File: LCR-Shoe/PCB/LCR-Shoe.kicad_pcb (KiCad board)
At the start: 2 copper layers, 65 x 65 mm, 26 parts, among them J1 USB_B, J2 USB_C_Receptacle, J3 USB_B_Mini, J4 USB_B_Micro, J5 Conn_01x01_Female, J6 Conn_01x01_Male, Q1 IRLML6402PbF, U1 LM2731YMF, U2 LTC4412xS6

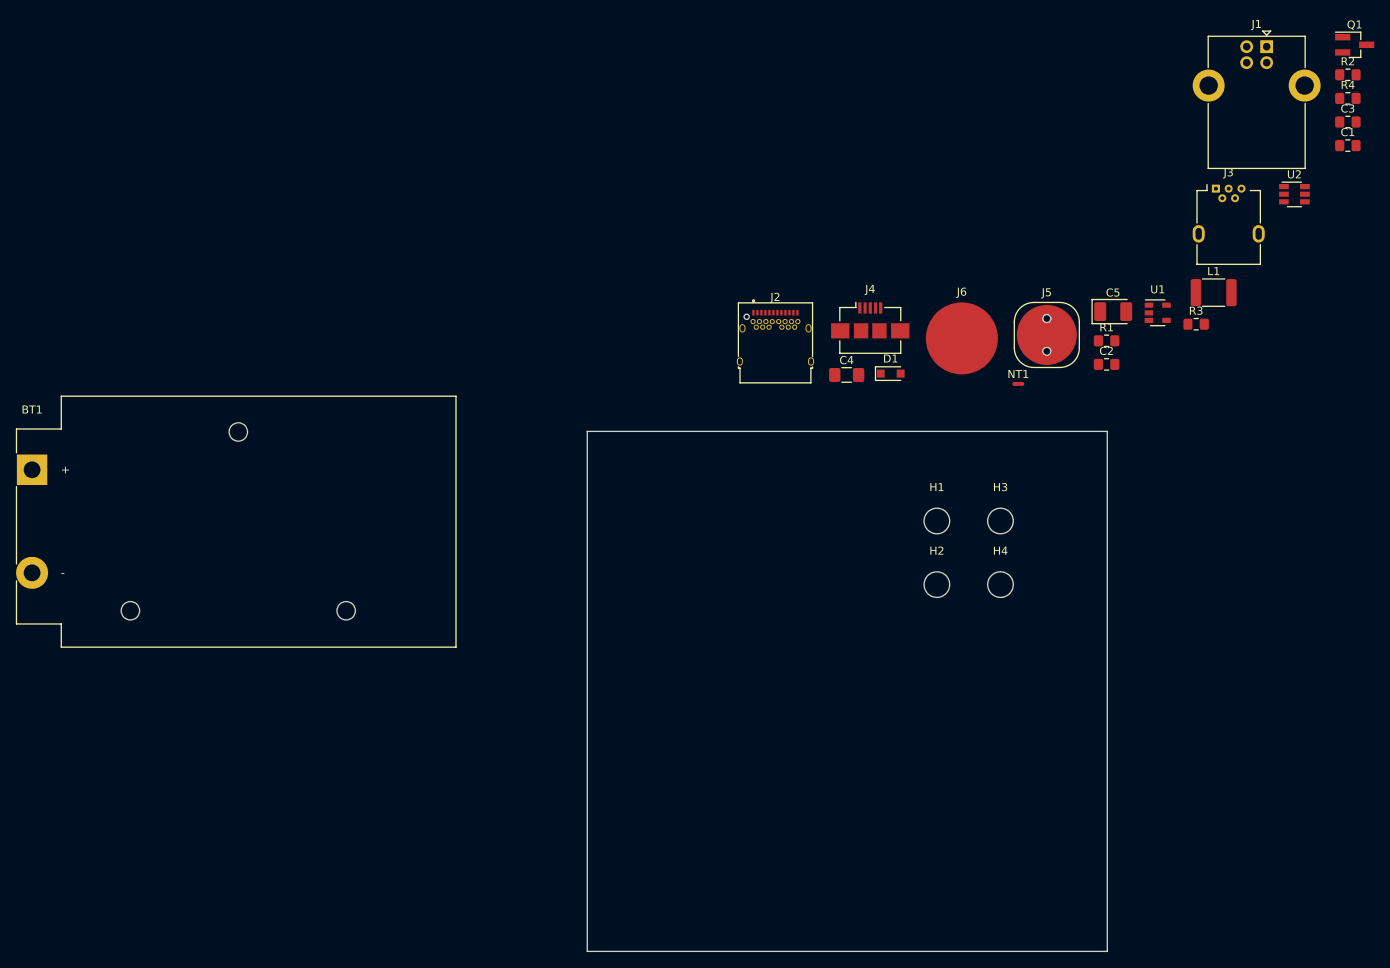
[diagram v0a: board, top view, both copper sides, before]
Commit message: All components laid out
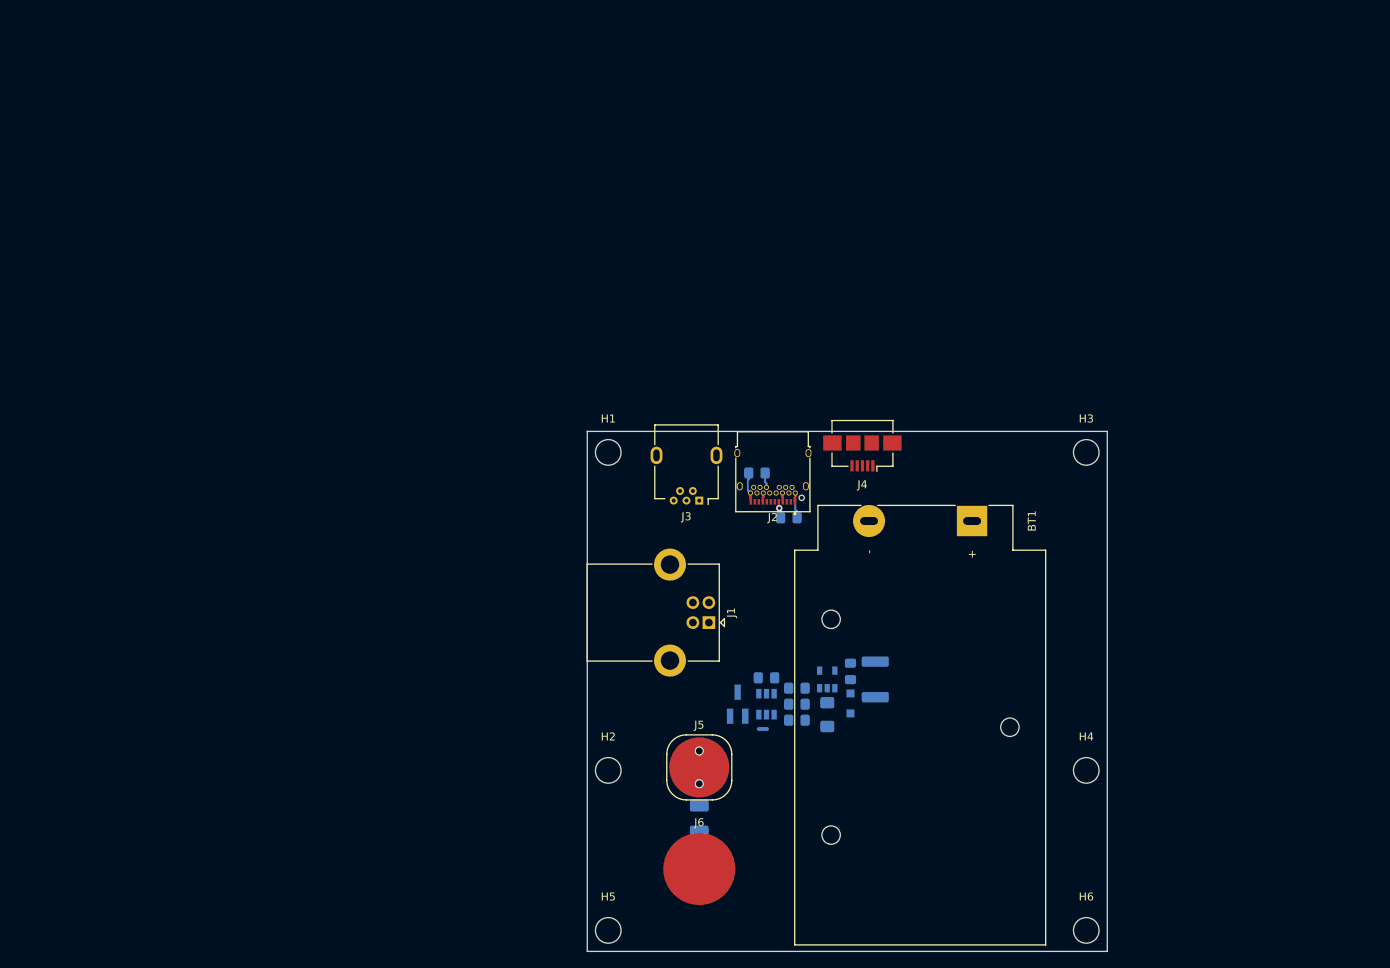
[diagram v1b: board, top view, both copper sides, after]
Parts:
- added H5: MountingHole, MountingHole:MountingHole_3.2mm_M3, F.Cu at (102.6, 162.4)
- added H6: MountingHole, MountingHole:MountingHole_3.2mm_M3, F.Cu at (162.4, 162.4)
- C1, C2, C3, C4, C5, D1, L1, NT1, Q1, R1, R2, R3, R4, U1, U2: moved to B.Cu
- moved BT1 117.7 mm to (148.1, 111.2), turned to 270 degrees
- moved Q1 112.9 mm to (118.8, 134.1), turned to 90 degrees
- moved R4 103.9 mm to (126.2, 136.1), turned to 180 degrees
- moved C3 100.5 mm to (122.4, 130.8)
- moved J1 100.2 mm to (115.2, 123.9), turned to 270 degrees
- moved U2 91.8 mm to (122.4, 134.1), turned to 270 degrees
- moved C1 90.5 mm to (132.9, 130.0), turned to 270 degrees
- moved R2 89.2 mm to (125.2, 110.8)
- moved C5 81.8 mm to (114.0, 148.4), turned to 270 degrees
- moved J3 75.4 mm to (114.0, 108.7), turned to 180 degrees
- moved J6 74.0 mm to (114.0, 154.7)
- moved J5 69.3 mm to (114.0, 142.0)
- moved R3 67.5 mm to (126.2, 132.1), turned to 180 degrees
- moved L1 64.2 mm to (136.0, 131.0), turned to 270 degrees
- moved U1 61.7 mm to (130.0, 131.0), turned to 90 degrees
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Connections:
- net Net-(J2-PadA5) renamed /USB_C-CC1
- net Net-(J2-PadB5) renamed /USB_C-CC2
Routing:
- net GND: track 0.00 -> 8.27 mm
- net +5V: track 0.00 -> 2.26 mm
- net /USB_C-CC1: track 0.00 -> 2.08 mm, vias 0 -> 1
- net /USB_C-CC2: track 0.00 -> 1.87 mm

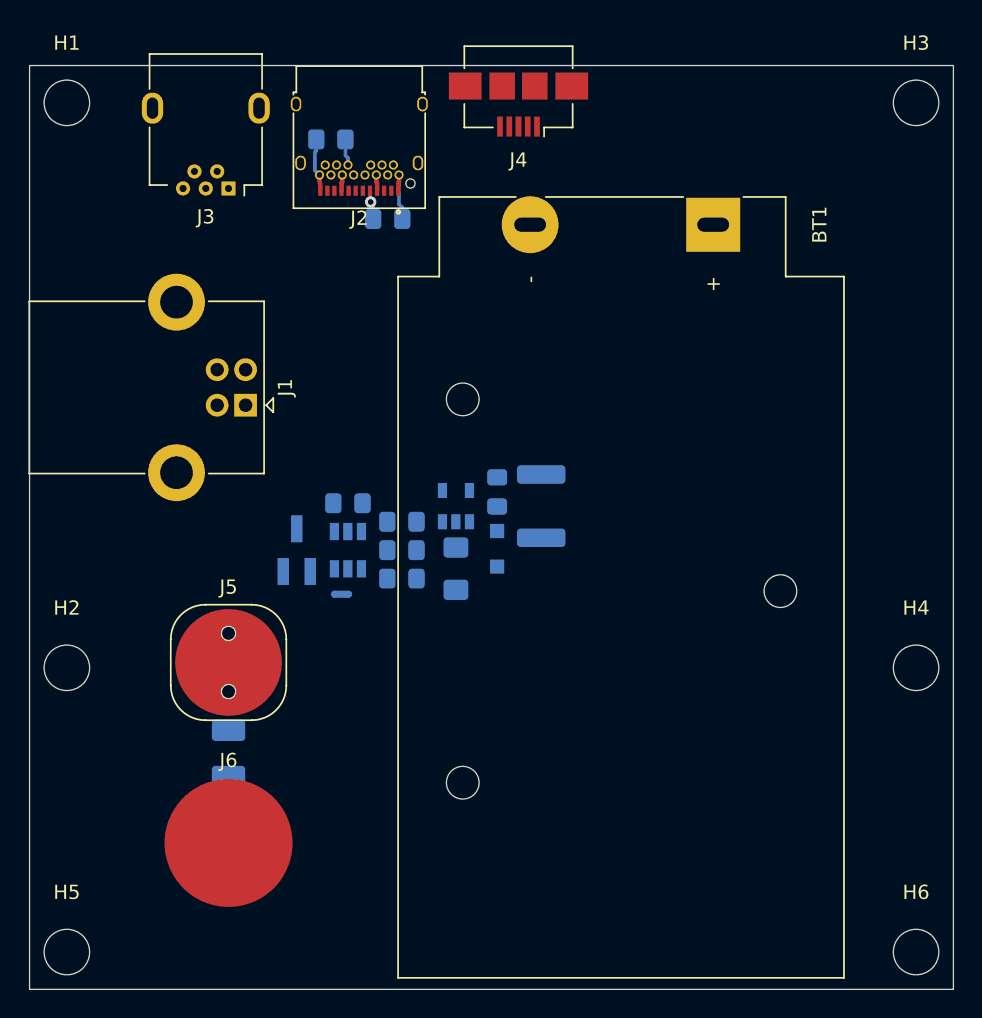
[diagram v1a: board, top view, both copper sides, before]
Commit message: Routing and positioning of the silk screen elements is finished
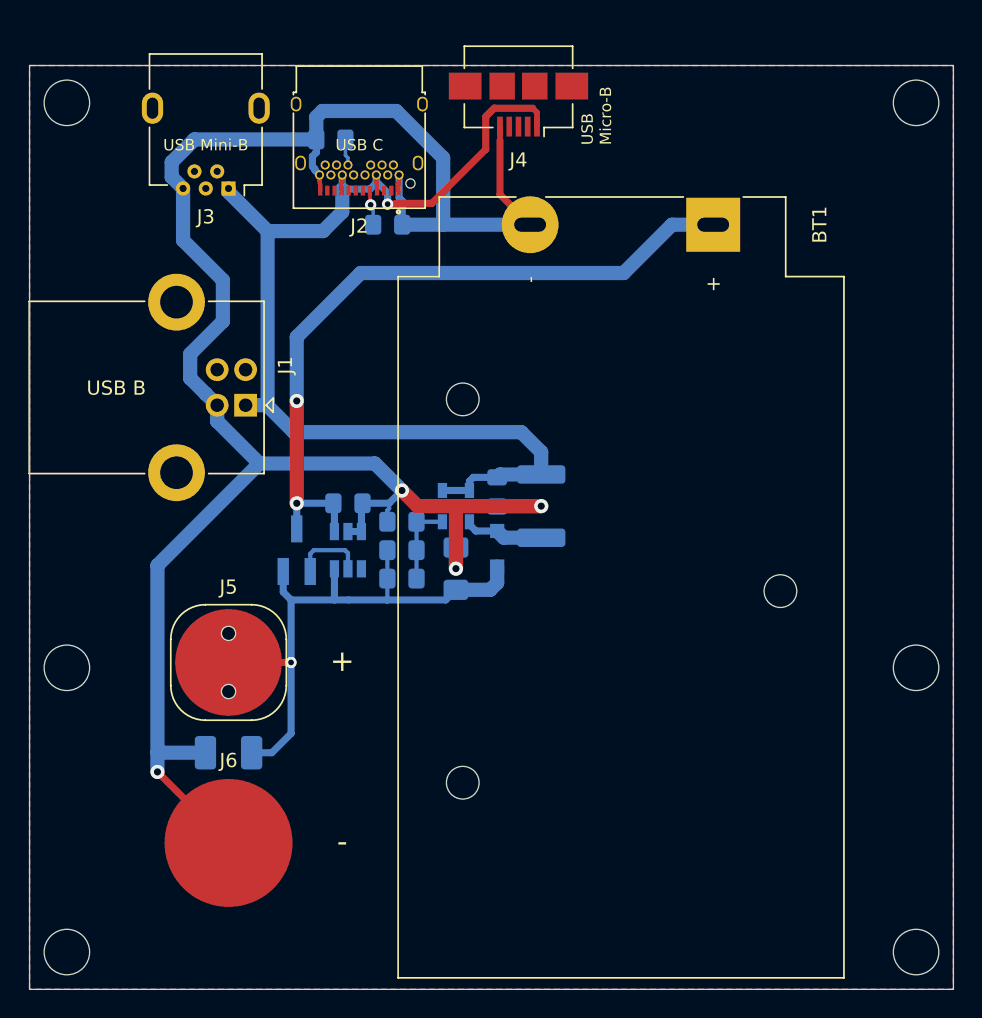
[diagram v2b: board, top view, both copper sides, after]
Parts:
- added ?: , , F.Cu at (148.2, 115.4)
- added REF**: OSHW-Logo2_14.6x12mm_SilkScreen, Symbol:OSHW-Logo2_14.6x12mm_SilkScreen, B.Cu at (145.2, 140.6)
- moved NT1 0.40 mm to (122.0, 137.6)
- moved R2 0.40 mm to (125.2, 111.2)
- moved C5 0.05 mm to (114.0, 148.3), turned to 180 degrees
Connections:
- J1 pad 5: Net-(J1-Pad5) -> (no net)
- J2 pad S1: Net-(J2-PadS1) -> (no net)
- J3 pad 6: Net-(J3-Pad6) -> (no net)
- J4 pad 6: Net-(J4-Pad6) -> (no net)
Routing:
- net GND: track 8.27 -> 155.3 mm, vias 0 -> 4
- net +5V: track 2.26 -> 79.9 mm, vias 0 -> 1
- net +9V: track 0.00 -> 50.7 mm, vias 0 -> 2
- net VCC: track 0.00 -> 24.6 mm, vias 0 -> 1
- net +10V: track 0.00 -> 15.6 mm
- net /FB: track 0.00 -> 5.83 mm
- net /SW: track 0.00 -> 5.60 mm
- net /G: track 0.00 -> 5.20 mm
- added copper zone on B.Cu, net GND
- added copper zone on F.Cu, net GND
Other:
- net class Min added: clearance 0.1, trace_width 0.1, via_dia 0.45, via_drill 0.2
- rule pad_to_mask_clearance: 0.051 -> 0
- rule solder_mask_min_width: 0.25 -> 0.1
- rule trace_min: 0.2 -> 0.1
- rule via_min_drill: 0.3 -> 0.2
- rule via_min_size: 0.4 -> 0.45
- board text added: "+"
- board text added: "-"
- board text added: "LCR-Shoe"
- board text added: "OHL v1.2"
- board text added: "Rev. 19/1"
- board text added: "USB B"
- board text added: "USB C"
- board text added: "USB Micro-B"
- board text added: "USB Mini-B"
- board text added: "http://michis-pla.net"

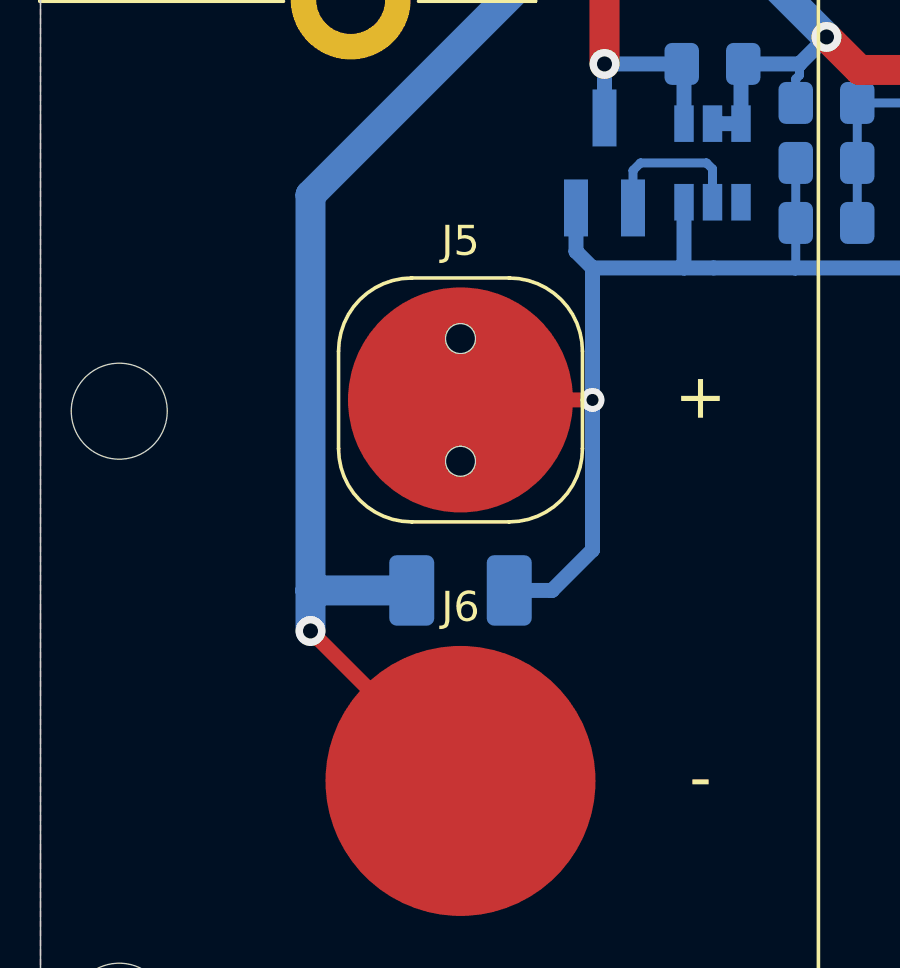
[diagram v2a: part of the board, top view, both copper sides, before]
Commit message: And there we have it: The first fixed bug!
The "battery connector" had swapped footprints. Both "simulate" a battery, and a 9 Volt battery has - on the receptacle (socket) and + on the plug (stud).

Time will tell if this was the only bug.
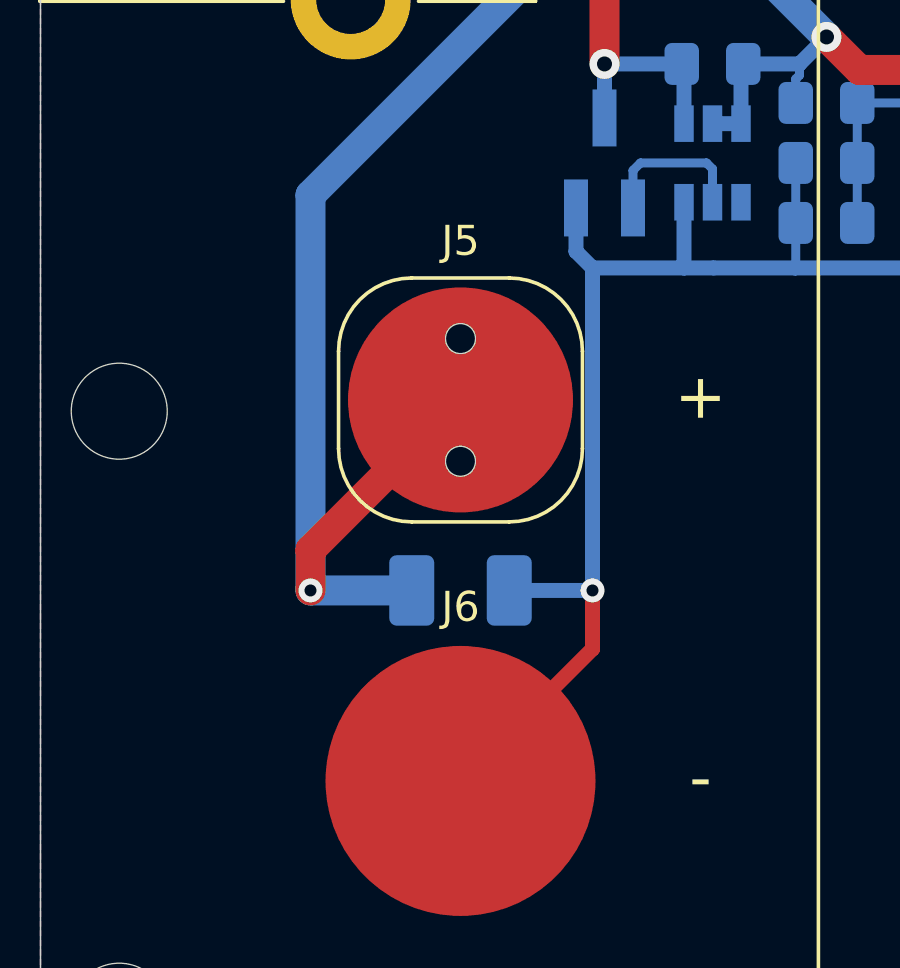
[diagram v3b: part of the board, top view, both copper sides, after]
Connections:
- J5 pad 1: VCC -> GND
- J6 pad 1: GND -> VCC
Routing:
- net VCC: track 24.6 -> 29.2 mm
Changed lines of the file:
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@@
     (thickness 1.6)
     (drawings 14)
-    (tracks 166)
+    (tracks 167)
     (zones 0)
     (modules 30)
@@
   )
   (setup
-    (last_trace_width 0.25)
+    (last_trace_width 1)
     (user_trace_width 0.1)
     (user_trace_width 0.3)
@@
     (mod_text_size 0.8 0.8)
     (mod_text_width 0.1)
-    (pad_size 4 4)
-    (pad_drill 2.3)
+    (pad_size 2.3 1.9)
+    (pad_drill 0)
     (pad_to_mask_clearance 0)
     (solder_mask_min_width 0.1)
@@
     (fp_line (start -4.57 4.57) (end -4.57 -4.57) (layer F.CrtYd) (width 0.05))
     (pad 1 smd circle (at 0 0) (size 7.5 7.5) (layers F.Cu F.Paste F.Mask)
-      (net 5 VCC))
+      (net 2 GND))
     (pad "" np_thru_hole circle (at 0 -2.045) (size 1 1) (drill 1) (layers *.Cu *.Mask)
       (clearance 0.001))
@@
     (fp_line (start -5 5) (end -5 -5) (layer F.CrtYd) (width 0.05))
     (pad 1 smd circle (at 0 0) (size 9 9) (layers F.Cu F.Paste F.Mask)
-      (net 2 GND))
+      (net 5 VCC))
   )
   (module Inductor_SMD:L_1812_4532Metric_Pad1.30x3.40mm_HandSolder (layer B.Cu)
@@
   (segment (start 125.175 131.3) (end 125.3 131.175) (width 0.3) (layer B.Cu) (net 2))
   (segment (start 125.175 132.1) (end 125.175 131.3) (width 0.3) (layer B.Cu) (net 2))
-  (via (at 109 149.7) (size 1) (drill 0.5) (layers F.Cu B.Cu) (net 2))
   (segment (start 116.16863 128) (end 109 135.16863) (width 1) (layer B.Cu) (net 2))
-  (segment (start 109 149.7) (end 114 154.7) (width 0.5) (layer F.Cu) (net 2))
   (segment (start 125.95 108.81) (end 125.95 108.25) (width 0.3) (layer F.Cu) (net 2))
   (segment (start 120.45 108.35) (end 120.42501 108.32501) (width 0.3) (layer F.Cu) (net 2))
@@
   (segment (start 111.6 105.2) (end 110 106.8) (width 1) (layer B.Cu) (net 2))
   (segment (start 112.375 148.35) (end 109 148.35) (width 1) (layer B.Cu) (net 2))
-  (segment (start 109 135.16863) (end 109 148.35) (width 1) (layer B.Cu) (net 2))
-  (segment (start 109 148.35) (end 109 149.7) (width 1) (layer B.Cu) (net 2))
+  (segment (start 109 135.16863) (end 109 148.3) (width 1) (layer B.Cu) (net 2))
+  (segment (start 109 148.3) (end 109 148.35) (width 1) (layer B.Cu) (net 2))
+  (via (at 109 148.35) (size 0.8) (drill 0.4) (layers F.Cu B.Cu) (net 2))
+  (segment (start 109 147) (end 109 148.35) (width 1) (layer F.Cu) (net 2))
+  (segment (start 114 142) (end 109 147) (width 1) (layer F.Cu) (net 2))
   (segment (start 121.95 108.81) (end 121.95 108.25) (width 0.3) (layer F.Cu) (net 3))
   (segment (start 122 108.2) (end 122 107.7) (width 0.3) (layer F.Cu) (net 3))
@@
   (segment (start 121.45 137.6) (end 118.4 137.6) (width 0.5) (layer B.Cu) (net 5))
   (segment (start 118.4 137.6) (end 117.85 137.05) (width 0.5) (layer B.Cu) (net 5))
-  (via (at 118.4 142) (size 0.8) (drill 0.4) (layers F.Cu B.Cu) (net 5))
-  (segment (start 114 142) (end 118.4 142) (width 0.5) (layer F.Cu) (net 5))
   (segment (start 118.4 142) (end 118.4 137.6) (width 0.5) (layer B.Cu) (net 5))
-  (segment (start 118.4 147) (end 118.4 142) (width 0.5) (layer B.Cu) (net 5))
-  (segment (start 115.625 148.35) (end 117.05 148.35) (width 0.5) (layer B.Cu) (net 5))
-  (segment (start 117.05 148.35) (end 118.4 147) (width 0.5) (layer B.Cu) (net 5))
+  (via (at 118.4 148.35) (size 0.8) (drill 0.4) (layers F.Cu B.Cu) (net 5))
+  (segment (start 118.4 142) (end 118.4 148.35) (width 0.5) (layer B.Cu) (net 5))
+  (segment (start 118.4 148.35) (end 115.625 148.35) (width 0.5) (layer B.Cu) (net 5))
+  (segment (start 118.4 150.3) (end 118.4 148.35) (width 0.5) (layer F.Cu) (net 5))
+  (segment (start 114 154.7) (end 118.4 150.3) (width 0.5) (layer F.Cu) (net 5))
   (segment (start 127.225 132.1) (end 127.225 134.1) (width 0.3) (layer B.Cu) (net 29))
   (segment (start 127.225 134.1) (end 127.225 136.1) (width 0.3) (layer B.Cu) (net 29))
